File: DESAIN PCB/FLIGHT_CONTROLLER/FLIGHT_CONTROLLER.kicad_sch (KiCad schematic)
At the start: 39 parts

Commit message: update PCB schematic
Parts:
- removed J?: Conn_01x03, symbol Connector_Generic:Conn_01x03
- added D4: D_Small, Diode_SMD:D_SMB_Handsoldering, symbol Device:D_Small
- added J12: RC TRANSMITTER, symbol Connector:Conn_01x05_Male
- added J13: TRANSMITTER, symbol Connector:Conn_01x04_Male
- added J14: GY-88A, symbol Connector_Generic:Conn_01x08
- added SW1: SW_DPDT_x2, Button_Switch_THT:SW_Push_2P2T_Toggle_CK_PVA2xxH4xxxxxxV2, symbol Switch:SW_DPDT_x2
- C10, C2: renamed from C?; footprint (none) -> Capacitor_Tantalum_SMD:CP_EIA-3216-18_Kemet-A_Pad1.58x1.35mm_HandSolder
- C11, C12, C13, C14, C3, C4, C6, C7, C8: renamed from C?; footprint (none) -> Capacitor_SMD:C_0805_2012Metric_Pad1.18x1.45mm_HandSolder
- D1: renamed from D?; footprint (none) -> Diode_SMD:D_SMB_Handsoldering
- F1, F2: renamed from F?; footprint (none) -> Fuse:Fuse_1812_4532Metric_Pad1.30x3.40mm_HandSolder
- SW2: renamed from SW?; footprint (none) -> Button_Switch_THT:SW_Tactile_SPST_Angled_PTS645Vx31-2LFS
- Y1: renamed from Y?; footprint (none) -> Crystal:Crystal_HC49-4H_Vertical
- gave numbers to parts that had none: 22
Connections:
- net +5V: now also F2.2, J10.2 (Pin_2), J11.2 (Pin_2), J4.2 (Pin_2), J5.2 (Pin_2), U3.20 (VCC), U3.4 (VCCIO), D4.1 (K), J13.4 (Pin_4), J14.1 (Pin_1)
- net +BATT: now also SW1.2 (B); no longer J6.1 (Pin_1), J7.1 (Pin_1), J8.1 (Pin_1), J9.1 (Pin_1)
- net D2: now also J12.1 (Pin_1)
- net D3: now also J4.3 (Pin_3)
- net D4: now also J12.2 (Pin_2)
- net D5: now also J12.3 (Pin_3)
- net D6: now also J12.4 (Pin_4)
- net D7: now also J12.5 (Pin_5)
- net D9: now also J10.3 (Pin_3)
- net GND: now also J10.1 (Pin_1), J11.1 (Pin_1), J4.1 (Pin_1), J5.1 (Pin_1), D4.2 (A), J13.1 (Pin_1), J14.3 (Pin_3)
- net I2C_+: now also J14.5 (Pin_5)
- net I2C_-: now also J14.4 (Pin_4)
- net UART_+: now also J13.3 (Pin_3)
- net UART_-: now also J13.2 (Pin_2)
- net VBUS: no longer F2.2, U3.20 (VCC), U3.4 (VCCIO)
- net VCC: now also J6.1 (Pin_1), J7.1 (Pin_1), J8.1 (Pin_1), J9.1 (Pin_1), SW1.1 (A)
- net D11: now reaches J11.3 (Pin_3)
- net D10: now reaches J5.3 (Pin_3)
- no-connect marks 10 -> 15
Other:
- note added: "BILA PANAS, GANTI KE SWITCHING REGULATOR"
- note added: "IMU SENSOR"
- note added: "PERIKSA DISSIPASI DAYA AMS1117"
- note added: "RADIO TRANSMITTER"
- note added: "THR=D2 ROLL=D6 PITCH=D5 YAW=D6 AUX/MODE=D7"
- moved on the sheet: C4, C5, C7, C9, D1, F1, J1, J10, J11, J2, J4, J5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

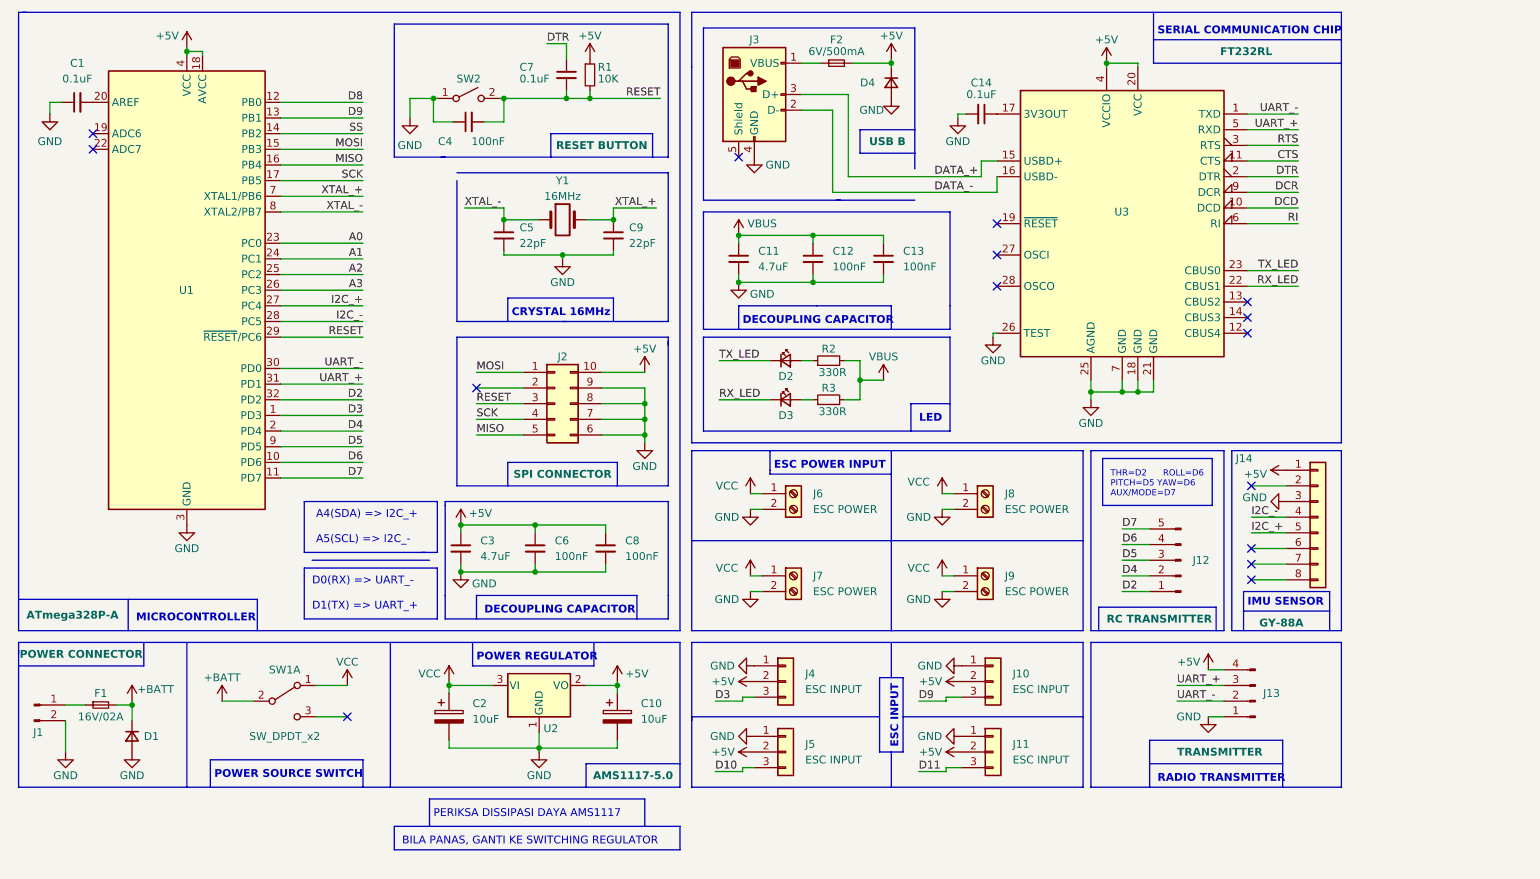
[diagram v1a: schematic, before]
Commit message: complete schematic
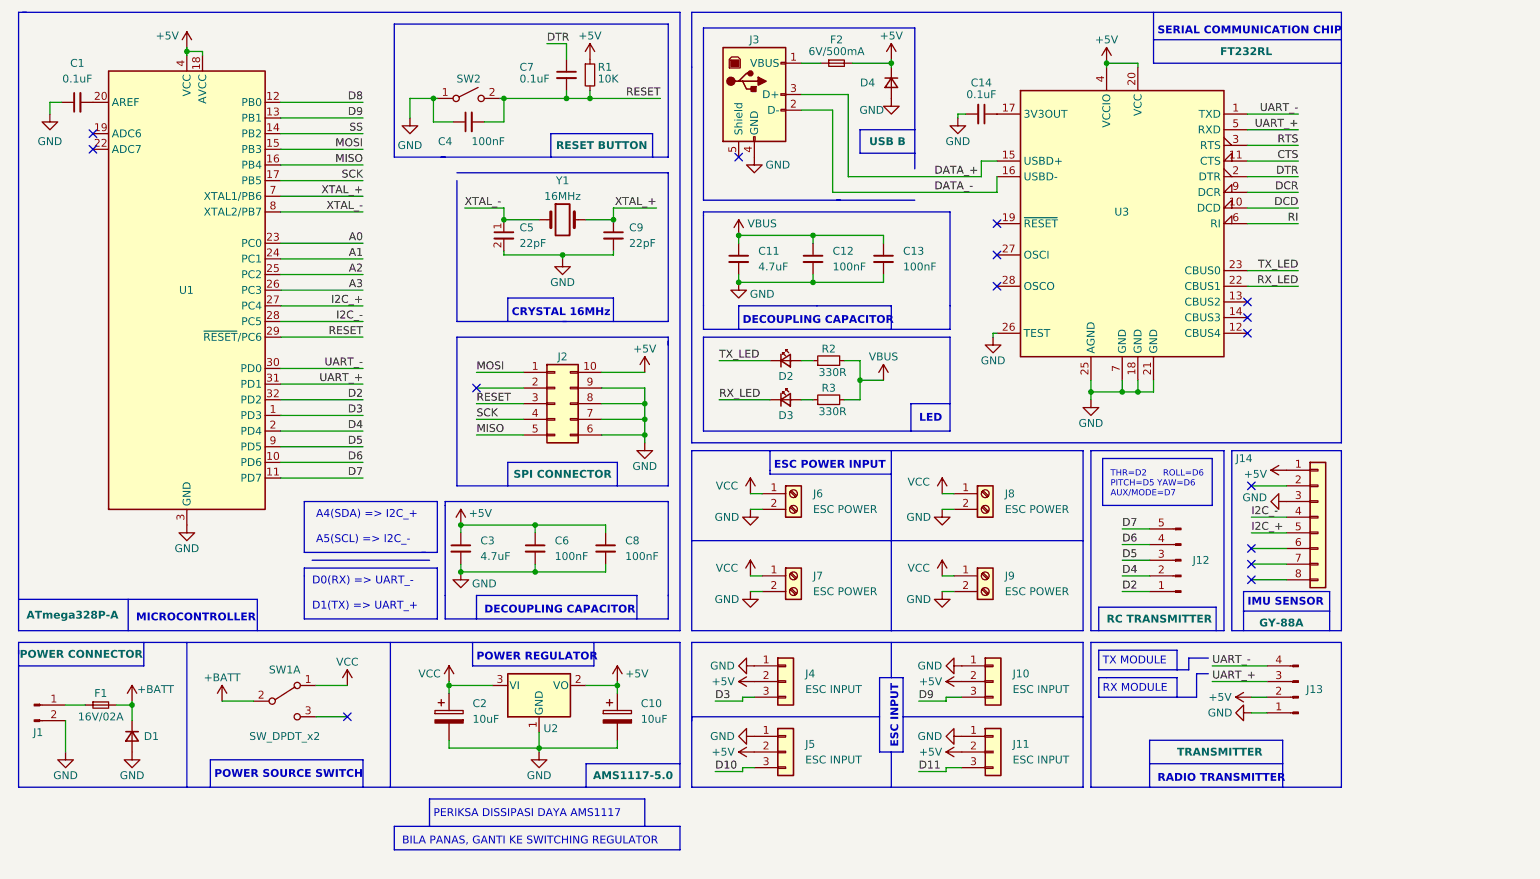
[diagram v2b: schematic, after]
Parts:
- C1, C5, C9: footprint (none) -> Capacitor_SMD:C_0805_2012Metric_Pad1.18x1.45mm_HandSolder
- D2, D3: footprint (none) -> LED_SMD:LED_0805_2012Metric_Pad1.15x1.40mm_HandSolder
- J10, J11, J4, J5: footprint (none) -> Connector_PinSocket_2.54mm:PinSocket_1x03_P2.54mm_Vertical
- J12: footprint (none) -> Connector_PinSocket_2.54mm:PinSocket_1x05_P2.54mm_Vertical
- J13: footprint (none) -> Connector_PinSocket_2.54mm:PinSocket_1x04_P2.54mm_Vertical
- J14: footprint (none) -> Connector_PinSocket_2.54mm:PinSocket_1x08_P2.54mm_Vertical
- J2: footprint (none) -> Connector_IDC:IDC-Header_2x05_P2.54mm_Vertical
- J6, J7, J8, J9: footprint (none) -> TerminalBlock_Phoenix:TerminalBlock_Phoenix_MKDS-1,5-2-5.08_1x02_P5.08mm_Horizontal
- R1, R2, R3: footprint (none) -> Resistor_SMD:R_0805_2012Metric_Pad1.20x1.40mm_HandSolder
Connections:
- net +5V: now also J13.2 (Pin_2); no longer J13.4 (Pin_4)
- net UART_-: now also J13.4 (Pin_4); no longer J13.2 (Pin_2)
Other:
- note added: "RX MODULE"
- note added: "TX MODULE"
- moved on the sheet: J13

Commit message: add PCB file
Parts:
- removed J2: SPI CONNECTOR, Connector_IDC:IDC-Header_2x05_P2.54mm_Vertical, symbol Connector_Generic:Conn_02x05_Counter_Clockwise
- added J2: SPI PROG, Connector_IDC:IDC-Header_2x05_P2.54mm_Vertical, symbol Connector_Generic:Conn_02x05_Odd_Even
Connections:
- net SS is gone; now on net D10: U1.14 (PB2)
- net VBUS is gone; now on net +5V: C11.1, C12.1, C13.1, R2.2, R3.2
- net +5V: now also J2.2 (Pin_2)
- net GND: now also J2.10 (Pin_10), J2.4 (Pin_4), J2.6 (Pin_6), J2.8 (Pin_8)
- net MISO: now also J2.9 (Pin_9)
- net MOSI: now also J2.1 (Pin_1)
- net RESET: now also J2.5 (Pin_5)
- net SCK: now also J2.7 (Pin_7)

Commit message: [Board] almost complete
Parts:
- added H1, H2, H3, H4: MountingHole, MountingHole:MountingHole_3.2mm_M3_ISO14580_Pad, symbol Mechanical:MountingHole
- added J15: FTDI BREAKOUT BOARD, Connector_PinHeader_2.54mm:PinHeader_1x06_P2.54mm_Vertical, symbol Connector:Conn_01x06_Male
- added J16: ESC POWER, TerminalBlock_Phoenix:TerminalBlock_Phoenix_MKDS-1,5-2-5.08_1x02_P5.08mm_Horizontal, symbol Connector:Screw_Terminal_01x02
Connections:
- net +5V: now also J15.4 (Pin_4)
- net GND: now also J15.6 (Pin_6), J16.1 (Pin_1)
- net UART_+: now also J15.2 (Pin_2)
- net UART_-: now also J15.3 (Pin_3)
- net at F1.1, J1.1 (Pin_1): now also J16.2 (Pin_2)
- no-connect marks 15 -> 17

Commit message: [Broad] just need to route PWM signal
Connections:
- no-connect marks 17 -> 16
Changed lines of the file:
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@@
   (no_connect (at 173.355 59.69))
   (no_connect (at 238.76 124.46))
-  (no_connect (at 131.445 38.735))
   (no_connect (at 26.67 34.925))
   (no_connect (at 214.63 92.075))

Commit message: [Board] complete, need review
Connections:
- net MOSI is gone; now on net D11: J2.1 (Pin_1), U1.15 (PB3)
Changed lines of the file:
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@@
     (stroke (width 0) (type default) (color 0 0 0 0))
   )
-  (wire (pts (xy 57.15 37.465) (xy 70.485 37.465))
+  (wire (pts (xy 57.15 37.465) (xy 73.025 37.465))
     (stroke (width 0) (type default) (color 0 0 0 0))
   )
@@
     (stroke (width 0) (type default) (color 0 0 0 0))
   )
+  (wire (pts (xy 73.025 43.815) (xy 81.915 43.815))
+    (stroke (width 0) (type default) (color 0 0 0 0))
+  )
   (wire (pts (xy 103.505 29.21) (xy 107.315 29.21))
     (stroke (width 0) (type default) (color 0 0 0 0))
@@
   )
   (polyline (pts (xy 211.455 86.36) (xy 229.235 86.36))
+    (stroke (width 0) (type default) (color 0 0 0 0))
+  )
+  (wire (pts (xy 73.025 37.465) (xy 73.025 43.815))
     (stroke (width 0) (type default) (color 0 0 0 0))
   )
@@
     (effects (font (size 1.27 1.27)) (justify left bottom))
   )
+  (label "D11" (at 81.915 43.815 180)
+    (effects (font (size 1.27 1.27)) (justify right bottom))
+  )
   (label "D2" (at 193.675 109.22 0)

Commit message: [Board] Review complete
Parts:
- removed J12: RC TRANSMITTER, Connector_PinSocket_2.54mm:PinSocket_1x05_P2.54mm_Vertical, symbol Connector:Conn_01x05_Male
- added J12: RC TRANSMITTER, Connector_PinSocket_2.54mm:PinSocket_1x07_P2.54mm_Vertical, symbol Connector_Generic:Conn_01x07
- J15: footprint Connector_PinHeader_2.54mm:PinHeader_1x06_P2.54mm_Vertical -> Connector_PinSocket_2.54mm:PinSocket_1x06_P2.54mm_Vertical
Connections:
- net +5V: now also J12.2 (Pin_2)
- net D2: now also J12.3 (Pin_3)
- net D4: now also J12.4 (Pin_4)
- net D5: now also J12.5 (Pin_5)
- net D6: now also J12.6 (Pin_6)
- net D7: now also J12.7 (Pin_7)
- net GND: now also J12.1 (Pin_1)
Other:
- note added: "THROT = D2 ROLL/AIL = D4 PITCH/ELEV = D5 YAW/RUD = D6 AUX/MODE = D7"
- note removed: "THR=D2 ROLL=D6 PITCH=D5 YAW=D6 AUX/MODE=D7"
- moved on the sheet: D1, F1, J1, J14, J16

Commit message: [board] correction
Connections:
- net GND: now also J1.1 (Pin_1); no longer J1.2 (Pin_2)
- net at F1.1, J16.2 (Pin_2): now also J1.2 (Pin_2); no longer J1.1 (Pin_1)
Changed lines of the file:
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@@
-    (stroke (width 0) (type default) (color 0 0 0 0))
-  )
-  (wire (pts (xy 22.225 123.825) (xy 26.67 123.825))
     (stroke (width 0) (type default) (color 0 0 0 0))
   )
@@
     (stroke (width 0) (type default) (color 0 0 0 0))
   )
+  (wire (pts (xy 22.352 126.238) (xy 25.4 126.238))
+    (stroke (width 0) (type default) (color 0 0 0 0))
+  )
   (wire (pts (xy 73.025 43.815) (xy 81.915 43.815))
     (stroke (width 0) (type default) (color 0 0 0 0))
@@
     (stroke (width 0) (type default) (color 0 0 0 0))
   )
-  (wire (pts (xy 26.67 123.825) (xy 26.67 127.635))
+  (wire (pts (xy 26.67 123.698) (xy 26.67 127.635))
     (stroke (width 0) (type default) (color 0 0 0 0))
   )
@@
     (stroke (width 0) (type default) (color 0 0 0 0))
   )
+  (wire (pts (xy 22.352 123.698) (xy 26.67 123.698))
+    (stroke (width 0) (type default) (color 0 0 0 0))
+  )
   (polyline (pts (xy 229.235 115.57) (xy 229.235 86.36))
     (stroke (width 0) (type default) (color 0 0 0 0))
@@
     (stroke (width 0) (type default) (color 0 0 0 0))
   )
-  (wire (pts (xy 25.4 126.365) (xy 25.4 133.35))
+  (wire (pts (xy 25.4 126.238) (xy 25.4 133.35))
     (stroke (width 0) (type default) (color 0 0 0 0))
   )
@@
   )
   (polyline (pts (xy 251.206 112.776) (xy 251.206 115.316))
-    (stroke (width 0) (type default) (color 0 0 0 0))
-  )
-  (wire (pts (xy 22.225 126.365) (xy 25.4 126.365))
     (stroke (width 0) (type default) (color 0 0 0 0))
   )
@@
     (pin "1")
   )
-  (symbol (lib_id "Connector:Conn_01x02_Male") (at 17.145 123.825 0) (unit 1)
-    (in_bom yes) (on_board yes)
-    (property "Reference" "J1" (id 0) (at 19.685 127.635 0))
-    (property "Value" "POWER CONNECTOR" (id 1) (at 24.765 119.38 0)
+  (symbol (lib_id "Connector:Conn_01x02_Male") (at 17.272 126.238 0) (mirror x) (unit 1)
+    (in_bom yes) (on_board yes)
+    (property "Reference" "J1" (id 0) (at 16.256 124.968 0))
+    (property "Value" "POWER CONNECTOR" (id 1) (at 24.638 119.634 0)
       (effects (font (size 1.27 1.27) bold))
     )
-    (property "Footprint" "Connector_AMASS:AMASS_XT60-M_1x02_P7.20mm_Vertical" (id 2) (at 17.145 123.825 0)
-      (effects (font (size 1.27 1.27)) hide)
-    )
-    (property "Datasheet" "~" (id 3) (at 17.145 123.825 0)
-      (effects (font (size 1.27 1.27)) hide)
-    )
+    (property "Footprint" "Connector_AMASS:AMASS_XT60-M_1x02_P7.20mm_Vertical" (id 2) (at 17.272 126.238 0)
+      (effects (font (size 1.27 1.27)) hide)
+    )
+    (property "Datasheet" "~" (id 3) (at 17.272 126.238 0)
+      (effects (font (size 1.27 1.27)) hide)
+    )
